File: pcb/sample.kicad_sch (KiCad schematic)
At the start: 14 parts, among them J1 Conn_Coaxial, J2 Conn_Coaxial

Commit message: apply output pos file
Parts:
- R1, R2, R3, R4, R5, R6: value ０ -> 0
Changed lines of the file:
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@@
 			)
 		)
-		(property "Value" "０"
+		(property "Value" "0"
 			(at 92.71 110.49 90)
 			(effects
@@
 			)
 		)
-		(property "Value" "０"
+		(property "Value" "0"
 			(at 115.57 110.49 90)
 			(effects
@@
 			)
 		)
-		(property "Value" "０"
+		(property "Value" "0"
 			(at 138.43 68.58 90)
 			(effects
@@
 			)
 		)
-		(property "Value" "０"
+		(property "Value" "0"
 			(at 92.71 68.58 90)
 			(effects
@@
 			)
 		)
-		(property "Value" "０"
+		(property "Value" "0"
 			(at 115.57 68.58 90)
 			(effects
@@
 			)
 		)
-		(property "Value" "０"
+		(property "Value" "0"
 			(at 138.43 110.49 90)
 			(effects

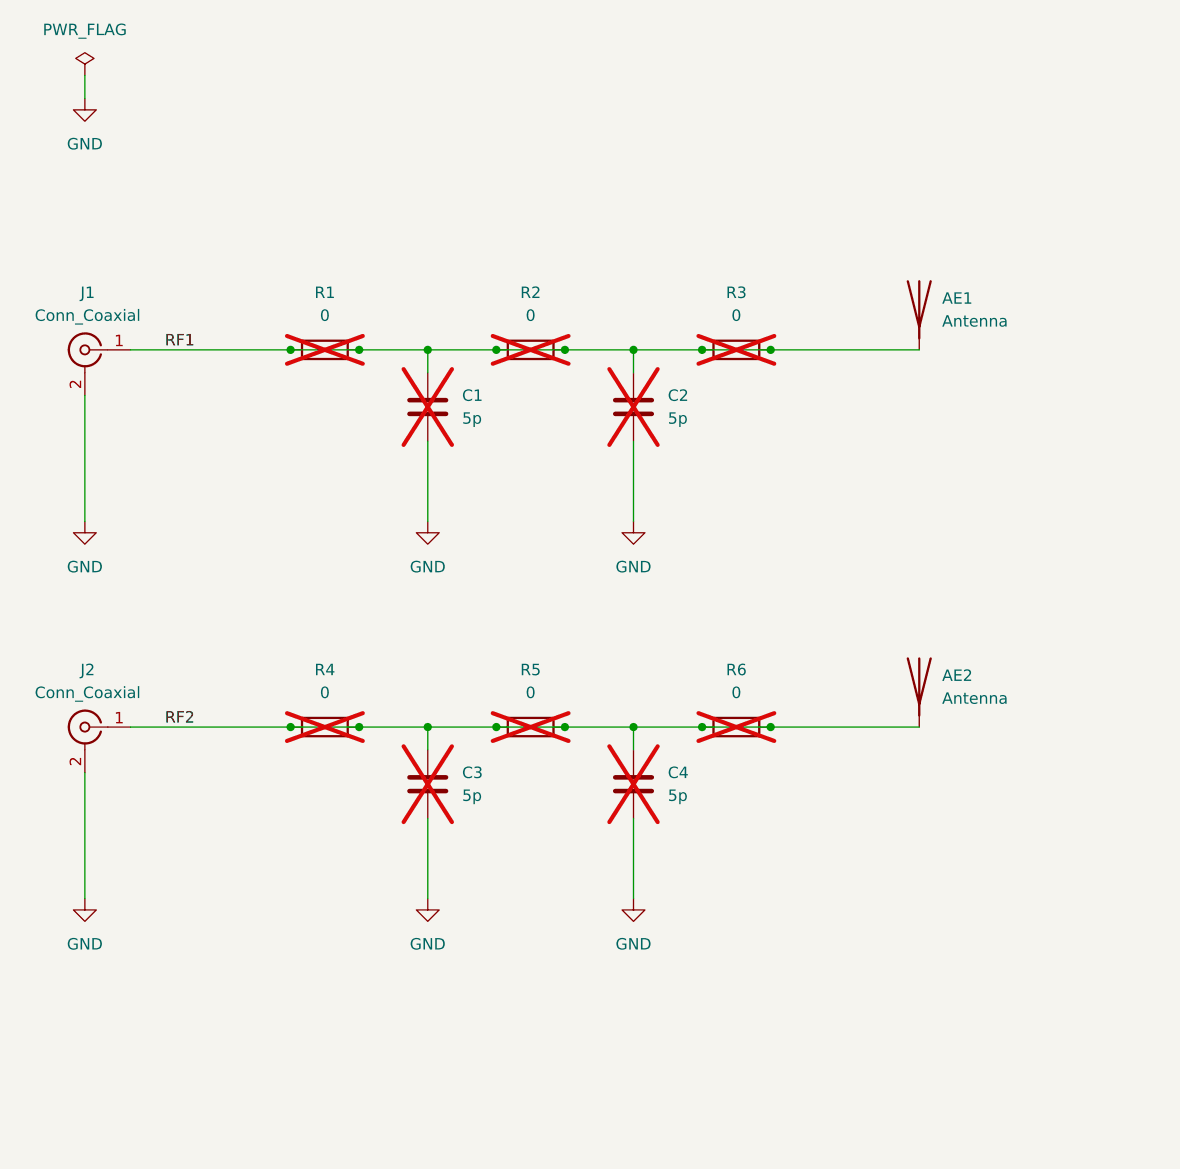
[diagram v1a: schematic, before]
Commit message: modify KiCAD 9.0 to 8.0
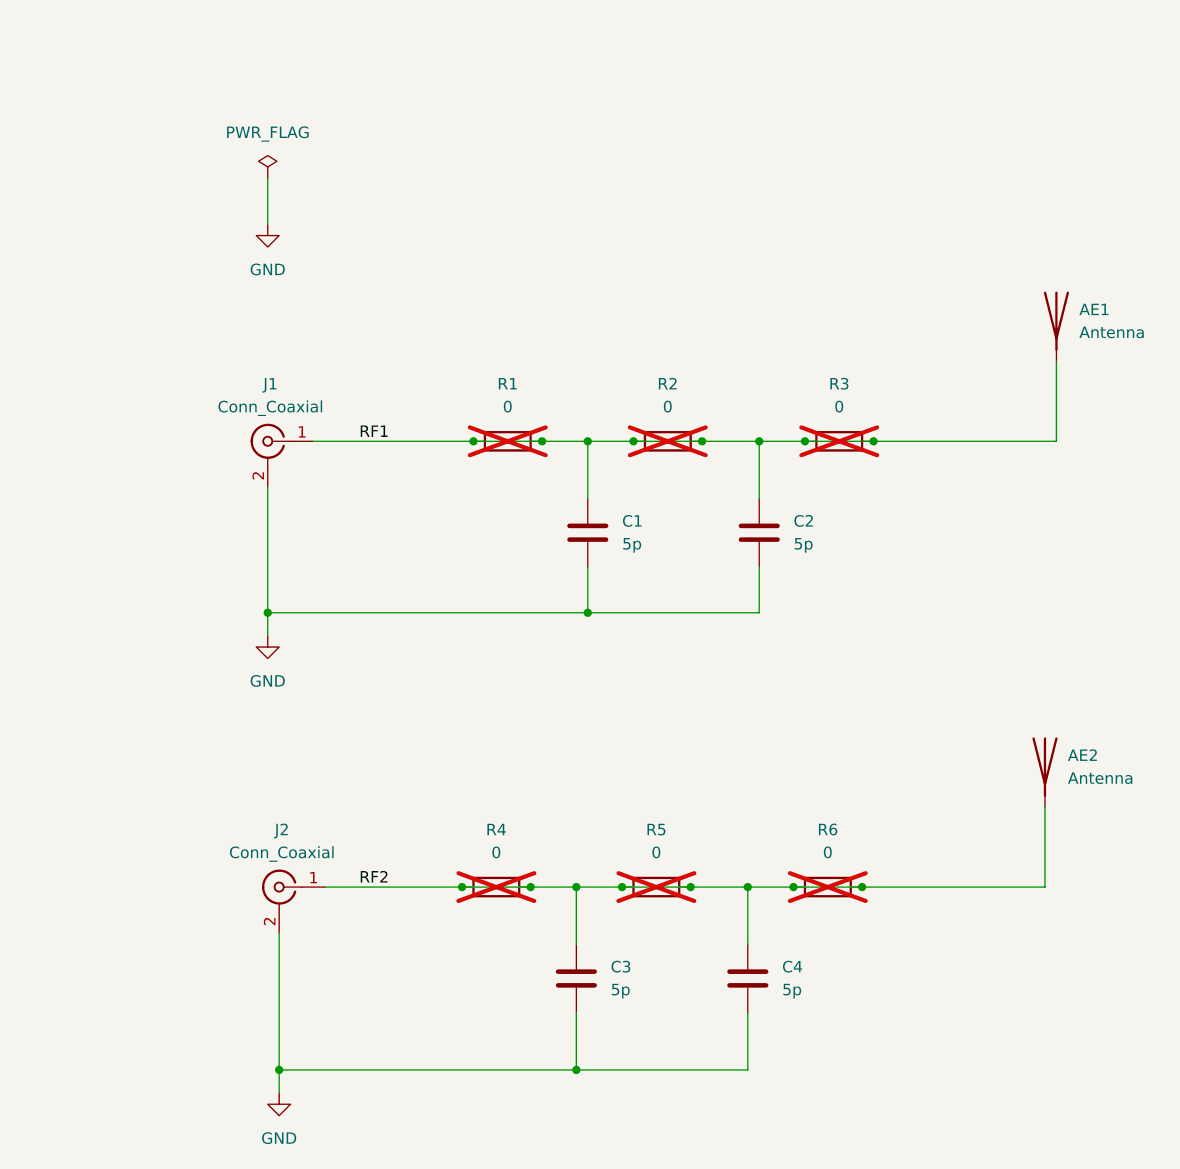
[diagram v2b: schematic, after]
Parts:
- AE1: footprint RF_Antenna:Antenna_Stub_1.0mm -> sample:Antenna_Stub_1.0mm
- AE2: footprint RF_Antenna:Antenna_Stub_0.5mm -> sample:Antenna_Stub_0.5mm
- C1, C2, C3, C4: now fitted
